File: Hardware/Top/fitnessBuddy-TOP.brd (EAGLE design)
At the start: 38 x 38 mm, 51 parts, among them SW1 SWITCH.MOM, SW2 SWITCH.MOM, U2 NRF52832_MODULE_MDBT42, U5 FT231XS

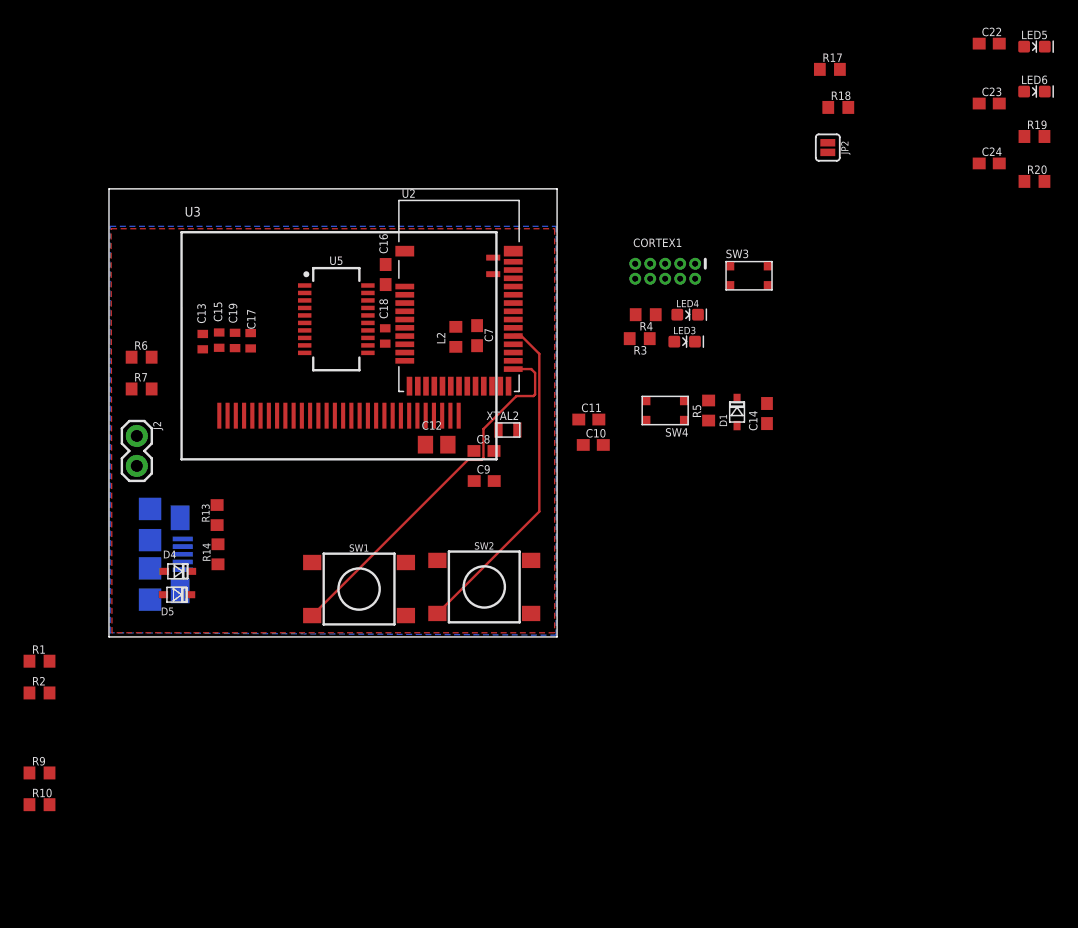
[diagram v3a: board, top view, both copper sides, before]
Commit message: Began routing top board
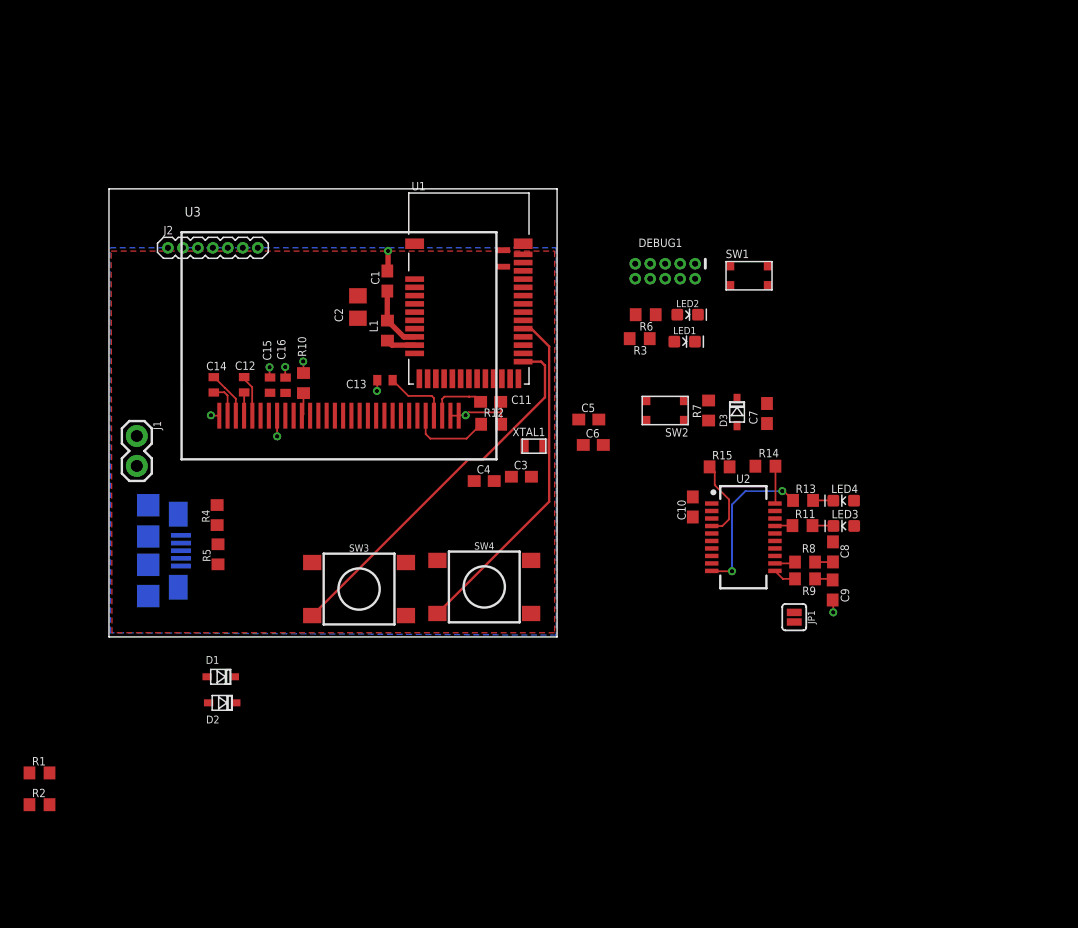
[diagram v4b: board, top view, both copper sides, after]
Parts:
- removed C17, C18, C19: 2.2uF, LinnesLab-Passives:C0402
- removed C22: 100n, LinnesLab-Passives:C0603
- removed C23, C24: 47p, LinnesLab-Passives:C0603
- removed D4, D5: (no value), LinnesLab-DiscreteSemi:USC
- removed JP2: (no value), LinnesLab-Switches:SMT-JUMPER_2_NO_SILK
- removed L2: 10u, LinnesLab-Passives:L0603
- removed LED5: RED, LinnesLab-LED:LED-0603
- removed LED6: YELLOW, LinnesLab-LED:LED-0603
- removed R17, R18: 27, LinnesLab-Passives:R0603
- removed R19, R20: 1k, LinnesLab-Passives:R0603
- removed U5: FT231XS, LinnesLab-DigitalIC:SSOP20_L
- removed USB2: USB.MICRO-BIGGERPADS, LinnesLab-Connectors:USB-MICRO-01.BIGGERPADS
- removed XTAL2: 32.768kHz, LinnesLab-Clocks:2-SMD.NOLEAD.2.0MMTO1.2MM
- added C1: 1u, LinnesLab-Passives:C0603
- added C2: 10u, LinnesLab-Passives:C0805
- added C3, C4: (no value), LinnesLab-Passives:C0603
- added C5, C6: 300p, LinnesLab-Passives:C0603
- added D2, D3: (no value), LinnesLab-DiscreteSemi:USC
- added J1: (no value), LinnesLab-Connectors:1X02
- added JP1: (no value), LinnesLab-Switches:SMT-JUMPER_2_NO_SILK
- added L1: 10u, LinnesLab-Passives:L0603
- added LED1: RED, LinnesLab-LED:LED-0603
- added LED2: BLUE, LinnesLab-LED:LED-0603
- added R11: 1k, LinnesLab-Passives:R0603
- added R12: 390k, LinnesLab-Passives:R0603
- added R15: 0, LinnesLab-Passives:R0603
- added R8: 27, LinnesLab-Passives:R0603
- added U1: NRF52832_MODULE_MDBT42, LinnesLab-Microcontrollers:BLE_MODULE_RAYTAC_MDBT42
- added USB1: USB.MICRO-BIGGERPADS, LinnesLab-Connectors:USB-MICRO-01.BIGGERPADS
- added XTAL1: 32.768kHz, LinnesLab-Clocks:2-SMD.NOLEAD.2.0MMTO1.2MM
- C10: value 300p -> 100n
- C11: value 300p -> 10uF
- C12: value 10u -> 2.2uF; device LinnesLab-Passives:C0805 -> LinnesLab-Passives:C0402
- C14: value 100n -> 2.2uF; device LinnesLab-Passives:C0603 -> LinnesLab-Passives:C0402
- C16: value 10uF -> 2.2uF; device LinnesLab-Passives:C0603 -> LinnesLab-Passives:C0402
- C7: value 1u -> 100n
- C8, C9: value (none) -> 47p
- J2: device LinnesLab-Connectors:1X02 -> LinnesLab-Connectors:1X07_1.27MM
- LED4: value BLUE -> YELLOW
- R1, R2: value 0 -> 10k
- R13: value 100k -> 1k
- R14: value 100k -> 0
- R4: value 1k -> 100k
- R5: value 10k -> 100k
- R6: value 10k -> 1k
- R7: value 390k -> 10k
- R9: value 10k -> 27
- SW1, SW2: value SWITCH.MOM -> (none); device LinnesLab-Switches:TACTILE_SWITCH_SMD_6.2MM_TALL -> LinnesLab-Switches:BUTTON-GULLWING
- SW3, SW4: value (none) -> SWITCH.MOM; device LinnesLab-Switches:BUTTON-GULLWING -> LinnesLab-Switches:TACTILE_SWITCH_SMD_6.2MM_TALL
- U2: value NRF52832_MODULE_MDBT42 -> FT231XS; device LinnesLab-Microcontrollers:BLE_MODULE_RAYTAC_MDBT42 -> LinnesLab-DigitalIC:SSOP20_L
- moved R9 67.0 mm to (59.0, 4.93), turned to 180 degrees
- moved R13 49.7 mm to (58.9, 11.6), turned to 0 degrees
- moved D1 49.2 mm to (9.47, -3.38), turned to 0 degrees
- moved R7 48.1 mm to (50.9, 19.2), turned to 90 degrees
- moved R14 47.0 mm to (55.7, 14.5), turned to 180 degrees
- moved C14 47.0 mm to (8.89, 21.4)
- moved R5 43.4 mm to (9.25, 7.01)
- moved R6 42.9 mm to (45.5, 27.3), turned to 180 degrees
- moved SW1 42.4 mm to (54.3, 30.6)
- moved SW3 42.4 mm to (21.2, 4.06)
- moved R10 42.2 mm to (16.5, 21.5), turned to 270 degrees
- moved R4 40.1 mm to (9.17, 10.3), turned to 90 degrees
- moved U2 31.6 mm to (53.8, 8.46), turned to 270 degrees
- moved C9 31.0 mm to (61.4, 3.99), turned to 270 degrees
- moved C8 30.8 mm to (61.4, 7.21), turned to 270 degrees
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- renumbered CORTEX1 to DEBUG1
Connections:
- net !CTS: now also JP1.2, U2.9; no longer JP2.2, U5.9
- net !DTR: now also U2.1; no longer U5.1
- net 3.3V: now also C10.2, C15.2, C16.2, C2.2, D3.-, J2.4, LED3.A, LED4.A, R1.2, R2.2, R7.2, U1.11, U2.14, U2.3; no longer C12.2, C17.2, C19.2, C22.2, D1.-, LED5.A, LED6.A, R10.2, R5.2, R9.2, U2.11, U5.14, U5.3
- net A4/BATT: now also R4.1, R5.2, U1.5; no longer R13.1, R14.2, U2.5
- net A6/TIA: now also J2.6, U1.7; no longer U2.7
- net A7/PPG: now also J2.7, U1.8; no longer U2.8
- net D11/SW1: now also SW3.A1, U1.25; no longer SW1.A1, U2.25
- net D15/SW2: now also SW4.A1, U1.29; no longer SW2.A1, U2.29
- net D16/CS.OLED: now also U1.30; no longer U2.30
- net D27/CHRG.STATUS: now also U1.4; no longer U2.4
- net D29/LED.CTRL: now also J2.5, U1.6; no longer U2.6
- net D3/RESET.OLED: now also U1.16; no longer U2.16
- net D4/DC.OLED: now also U1.17; no longer U2.17
- net D5/CD1: now also U1.18; no longer U2.18
- net D7/SD.CS: now also U1.20; no longer U2.20
- net DFU: now also SW1.3, U1.34; no longer SW3.3, U2.34
- net DTR: now also C7.1; no longer C14.1
- net FRST: now also U1.38; no longer U2.38
- net FT3V3: now also U2.13; no longer U5.13
- net GND: now also C1.2, C10.1, C11.1, C13.1, C15.1, C2.1, C3.1, C4.2, C5.2, C6.2, J1.1, J2.3, JP1.1, LED1.C, LED2.C, R10.1, R12.2, R5.1, SW1.1, SW2.3, SW3.B1, SW3.B2, SW4.B1, SW4.B2, U1.1, U1.12, U1.24, U1.39, U2.16, U2.6, USB1.5, USB1.S1, USB1.S2, USB1.S3, USB1.S4, USB1.S5, USB1.S6; no longer C10.2, C11.2, C12.1, C17.1, C18.1, C19.1, C22.1, C23.2, C24.1, C7.2, J2.1, JP2.1, LED3.C, LED4.C, R14.1, R6.1, R7.2, SW1.B1, SW1.B2, SW2.B1, SW2.B2, SW3.1, SW4.3, U2.1, U2.12, U2.24, U2.39, U5.16, U5.6, USB2.5, USB2.S1, USB2.S2, USB2.S3, USB2.S4, USB2.S5, USB2.S6
- net LED1: now also U1.31; no longer U2.31
- net LED2: now also R6.2, U1.33; no longer R4.2, U2.33
- net MISO: now also U1.28; no longer U2.28
- net MOSI: now also U1.27; no longer U2.27
- net N$1: now also R10.2; no longer R6.2
- net N$10: now also LED2.A, R6.1; no longer LED4.A, R4.1
- net N$11: now also L1.1, U1.10; no longer L2.1, U2.10
- net N$12: now also C1.1, L1.2, U1.9; no longer C7.1, L2.2, U2.9
- net N$13: now also C11.2; no longer C16.2
- net N$15: now also C13.2; no longer C18.2
- net N$2: now also R12.1; no longer R7.1
- net N$23: now also R8.2, U2.12; no longer R17.2, U5.12
- net N$24: now also R9.2, U2.11; no longer R18.2, U5.11
- net N$25: now also LED3.C, R11.2; no longer LED5.C, R19.2
- net N$26: now also LED4.C, R13.2; no longer LED6.C, R20.2
- net N$3: now also C14.2; no longer C13.2
- net N$4: now also C3.2, U1.13, XTAL1.P$1; no longer C8.2, U2.13, XTAL2.P$1
- net N$5: now also C14.1; no longer C13.1
- net N$6: now also C4.1, U1.14, XTAL1.P$2; no longer C9.1, U2.14, XTAL2.P$2
- net N$7: now also C12.2; no longer C15.2
- net N$8: now also C12.1; no longer C15.1
- net N$9: now also LED1.A; no longer LED3.A
- net P0.09/NFC1: now also C5.1, U1.22; no longer C11.1, U2.22
- net P0.10/NFC2: now also C6.1, U1.23; no longer C10.1, U2.23
- net RESET: now also C7.2, D3.+, R7.1, SW2.1, U1.35; no longer C14.2, D1.+, R5.1, SW4.1, U2.35
- net RXD.FT: now also R15.1, U2.4; no longer R2.1, U5.4
- net RXD.NRF: now also R14.2, U1.21; no longer R1.2, U2.21
- net RXLED: now also R11.1, U2.17; no longer R19.1, U5.17
- net SCK: now also U1.26; no longer U2.26
- net SCL: now also J2.2, R2.1, U1.3; no longer R10.1, U2.3
- net SDA: now also J2.1, R1.1, U1.2; no longer R9.1, U2.2
- net SWCLK: now also U1.36; no longer U2.36
- net SWDIO: now also U1.37; no longer U2.37
- net SWO: now also U1.32; no longer U2.32
- net TXD.FT: now also R14.1, U2.20; no longer R1.1, U5.20
- net TXD.NRF: now also R15.2, U1.19; no longer R2.2, U2.19
- net TXLED: now also R13.1, U2.10; no longer R20.1, U5.10
- net USB+: now also C9.1, R9.1, USB1.3; no longer C23.1, R18.1, USB2.3
- net USB-: now also C8.2, R8.1, USB1.2; no longer C24.2, R17.1, USB2.2
- net VIN: now also D1.-, D2.-; no longer D4.-, D5.-
- net VLIPO: now also D1.+, J1.2, R4.2; no longer D4.+, J2.2, R13.2
- net V_USB: now also D2.+, U2.15, USB1.1; no longer D5.+, U5.15, USB2.1
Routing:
- net GND: track 0.00 -> 15.3 mm, vias 0 -> 9
- net TXLED: track 0.00 -> 13.4 mm, vias 0 -> 2
- net N$2: track 0.00 -> 6.93 mm
- net RXD.FT: track 0.00 -> 6.83 mm
- net N$15: track 0.00 -> 5.63 mm
- net N$12: track 0.00 -> 5.39 mm
- net N$13: track 0.00 -> 4.94 mm
- net N$5: track 0.00 -> 4.11 mm
- net N$8: track 0.00 -> 3.56 mm
- net TXD.FT: track 0.00 -> 3.18 mm
- net N$3: track 0.00 -> 3.00 mm
- net N$11: track 0.00 -> 2.46 mm
- net N$24: track 0.00 -> 1.98 mm
- net N$7: track 0.00 -> 1.97 mm
- net N$1: track 0.00 -> 1.97 mm
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
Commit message: routed top board
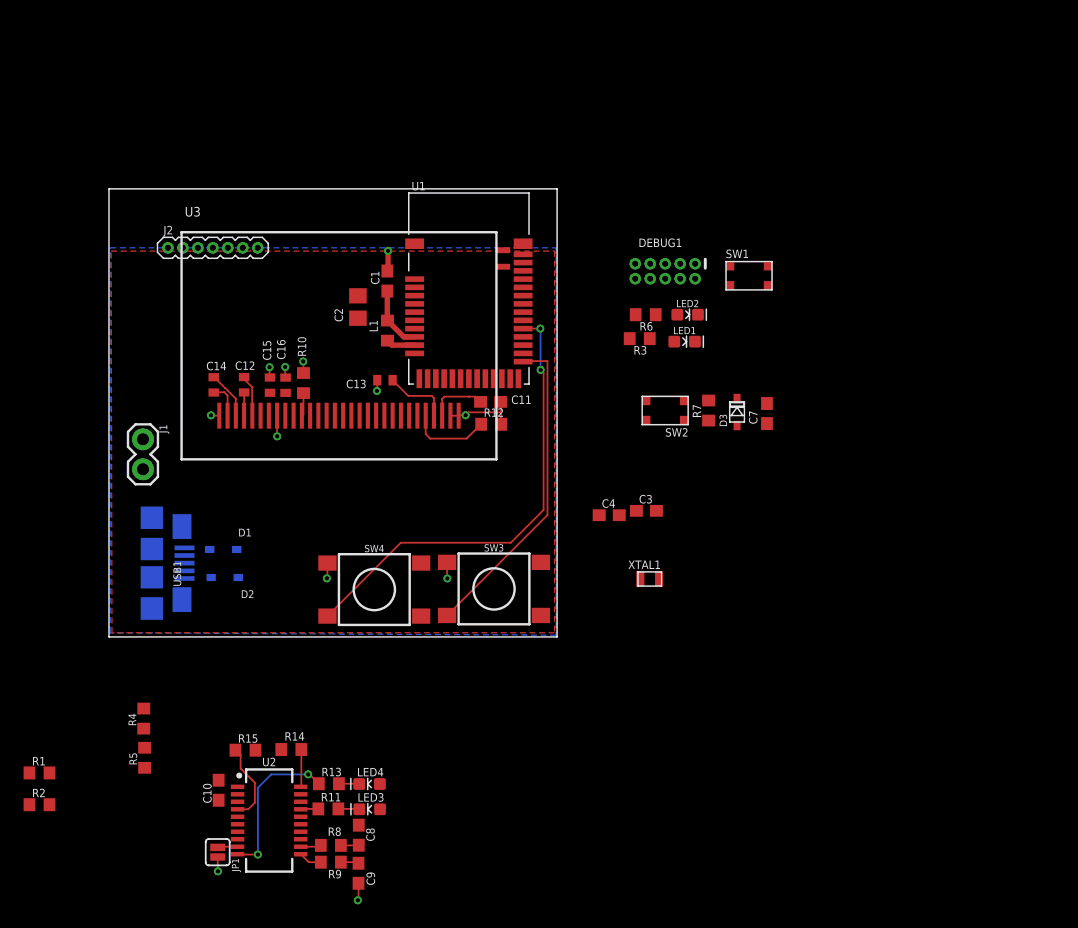
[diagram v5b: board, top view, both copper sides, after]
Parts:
- removed C5, C6: 300p, LinnesLab-Passives:C0603
- moved JP1 52.8 mm to (9.22, -18.3), turned to 90 degrees
- moved C10 46.8 mm to (9.30, -13.0)
- moved C8 46.8 mm to (21.2, -16.8)
- moved C9 46.8 mm to (21.2, -20.0)
- moved LED3 46.8 mm to (22.1, -14.6)
- moved LED4 46.8 mm to (22.1, -12.5)
- moved R11 46.8 mm to (18.6, -14.6)
- moved R13 46.8 mm to (18.7, -12.4)
- moved R14 46.8 mm to (15.5, -9.55)
- moved R15 46.8 mm to (11.6, -9.60)
- moved R8 46.8 mm to (18.8, -17.7)
- moved R9 46.8 mm to (18.8, -19.1)
- moved U2 46.8 mm to (13.6, -15.6)
- moved R4 18.3 mm to (2.95, -6.92)
- moved R5 18.3 mm to (3.03, -10.2)
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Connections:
- net GND: no longer C5.2, C6.2
- net P0.09/NFC1: no longer C5.1
- net P0.10/NFC2: no longer C6.1
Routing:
- net D15/SW2: track 29.5 -> 39.7 mm, vias 0 -> 2
- net D11/SW1: track 32.1 -> 27.2 mm
- net GND: track 15.3 -> 19.7 mm, vias 9 -> 12
- net !CTS: track 0.00 -> 1.71 mm

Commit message: Reorganized top and bottom boards, went back and rerouted some of top board (basically did take 005 and take 006)
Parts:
- moved C3 30.6 mm to (17.1, 21.8), turned to 270 degrees
- moved XTAL1 30.5 mm to (20.2, 21.5), turned to 90 degrees
- moved C4 26.5 mm to (18.5, 21.8), turned to 90 degrees
- moved C10 25.4 mm to (1.41, 11.1)
- moved C9 25.1 mm to (13.0, 3.71), turned to 90 degrees
- moved R8 24.2 mm to (10.6, 5.04)
- moved U2 24.2 mm to (5.38, 7.15)
- moved LED3 24.2 mm to (13.9, 8.10)
- moved LED4 24.2 mm to (13.9, 10.2)
- moved R11 24.2 mm to (10.4, 8.13)
- moved R13 24.2 mm to (10.4, 10.3)
- moved R15 24.0 mm to (3.81, 13.2)
- moved R14 23.9 mm to (9.00, 13.5), turned to 0 degrees
- moved C8 23.5 mm to (14.8, 5.79)
- moved R9 23.4 mm to (10.4, 2.77)
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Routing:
- net D15/SW2: track 39.7 -> 0.76 mm, vias 2 -> 0
- net RESET: track 0.00 -> 27.3 mm
- net D11/SW1: track 27.2 -> 0.03 mm
- net USB-: track 1.52 -> 24.5 mm, vias 0 -> 1
- net USB+: track 1.53 -> 17.9 mm, vias 0 -> 1
- net GND: track 19.7 -> 35.3 mm, vias 12 -> 19
- net VLIPO: track 0.00 -> 13.3 mm
- net TXLED: track 13.4 -> 0.08 mm, vias 2 -> 0
- net SWO: track 0.00 -> 12.5 mm, vias 0 -> 1
- net LED2: track 0.00 -> 9.65 mm
- net N$4: track 0.00 -> 8.43 mm
- net SWCLK: track 0.00 -> 8.42 mm
- net N$6: track 0.00 -> 7.02 mm
- net SWDIO: track 0.00 -> 6.62 mm, vias 0 -> 1
- net LED1: track 0.00 -> 5.96 mm
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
